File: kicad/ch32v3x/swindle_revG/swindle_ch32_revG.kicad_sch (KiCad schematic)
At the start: 34 parts, among them J1 jtag, J2 Conn_01x03_Socket, J2_DFU1 con2, J3 Dbg, J4 USB, J5 Debug port, U1 CH32V303RCT6, U2 LM1117-3.3, U3 3V->VTREF, U4 VTREF->3V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

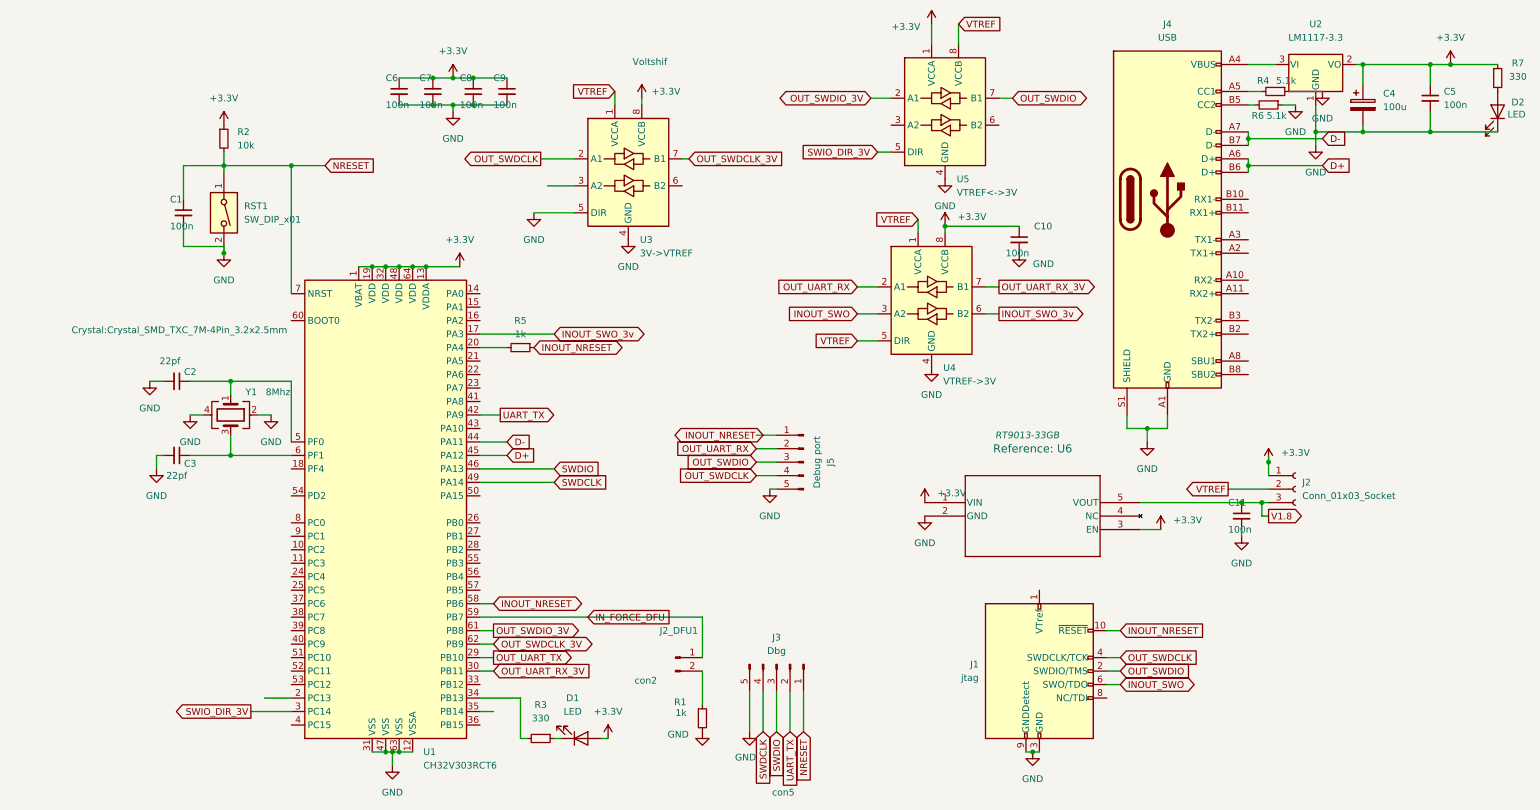
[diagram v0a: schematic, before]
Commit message: RP2040 : Add USE_RP2040 option to use the new PCB Kicad : RP2040 carrier layout mon : add mon enablereset to make exec from RAM work with vscode. That ignores the reset command sent by cortexdebug Misc : dont hardcode the target in the attach/vAttch command to 1.  Actually read the value.
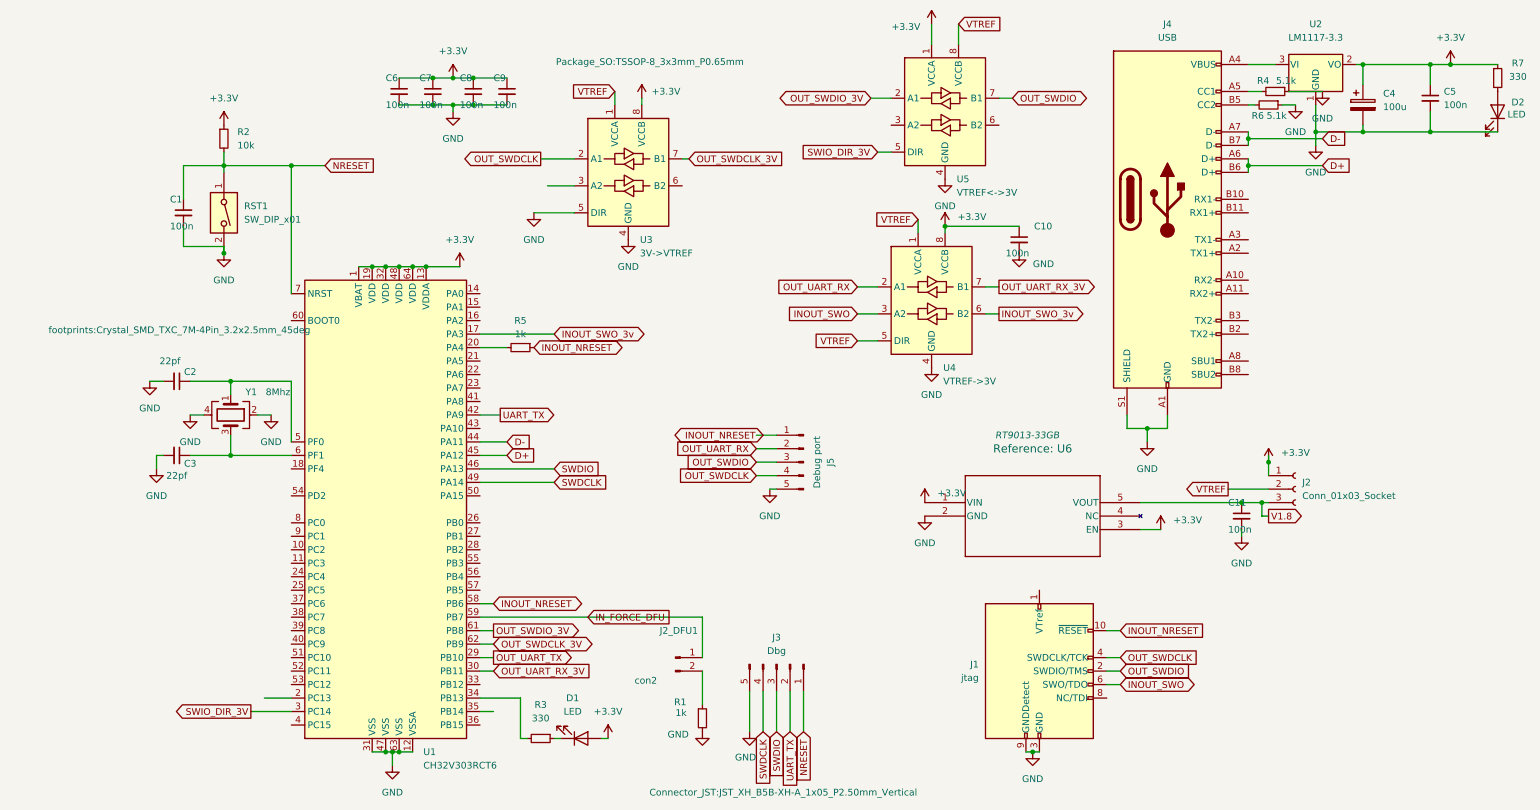
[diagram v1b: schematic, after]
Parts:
- J3: footprint con5 -> Connector_JST:JST_XH_B5B-XH-A_1x05_P2.50mm_Vertical
- J5: footprint Con5 -> Connector_JST:JST_XH_B5B-XH-A_1x05_P2.50mm_Vertical
- U3: footprint Voltshif -> Package_SO:TSSOP-8_3x3mm_P0.65mm
- U4, U5: footprint Package_SO:VSSOP-8_2.3x2mm_P0.5mm -> Package_SO:TSSOP-8_3x3mm_P0.65mm
- Y1: footprint Crystal:Crystal_SMD_TXC_7M-4Pin_3.2x2.5mm -> footprints:Crystal_SMD_TXC_7M-4Pin_3.2x2.5mm_45deg
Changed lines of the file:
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@@
 			)
 		)
-		(property "Footprint" "Con5"
+		(property "Footprint" "Connector_JST:JST_XH_B5B-XH-A_1x05_P2.50mm_Vertical"
 			(at 147.828 112.268 0)
 			(effects
@@
 			)
 		)
-		(property "Footprint" "Package_SO:VSSOP-8_2.3x2mm_P0.5mm"
+		(property "Footprint" "Package_SO:TSSOP-8_3x3mm_P0.65mm"
 			(at 175.26 46.99 0)
 			(effects
@@
 		)
 		(instances
-			(project "lnBMP_ch32_revF_5pins_prot"
+			(project "swindle_ch32_revG"
 				(path "/fbe443d6-6d74-4abc-9dee-16e0160553bc"
 					(reference "U5")
@@
 			)
 		)
-		(property "Footprint" "Voltshif"
+		(property "Footprint" "Package_SO:TSSOP-8_3x3mm_P0.65mm"
 			(at 118.364 23.622 0)
 			(effects
@@
 		)
 		(instances
-			(project "lnBMP_ch32_revF_5pins_prot"
+			(project "swindle_ch32_revG"
 				(path "/fbe443d6-6d74-4abc-9dee-16e0160553bc"
 					(reference "#PWR032")
@@
 		)
 		(instances
-			(project "lnBMP_ch32_revF_5pins_prot"
+			(project "swindle_ch32_revG"
 				(path "/fbe443d6-6d74-4abc-9dee-16e0160553bc"
 					(reference "#PWR026")
@@
 		)
 		(instances
-			(project "lnBMP_ch32_revF_5pins_prot"
+			(project "swindle_ch32_revG"
 				(path "/fbe443d6-6d74-4abc-9dee-16e0160553bc"
 					(reference "#PWR028")
@@
 		)
 		(instances
-			(project "lnBMP_ch32_revF_5pins_prot"
+			(project "swindle_ch32_revG"
 				(path "/fbe443d6-6d74-4abc-9dee-16e0160553bc"
 					(reference "C10")
@@
 		)
 		(instances
-			(project "lnBMP_ch32_revF_5pins_prot"
+			(project "swindle_ch32_revG"
 				(path "/fbe443d6-6d74-4abc-9dee-16e0160553bc"
 					(reference "#PWR030")
@@
 		)
 		(instances
-			(project "lnBMP_ch32_revF_5pins_prot"
+			(project "swindle_ch32_revG"
 				(path "/fbe443d6-6d74-4abc-9dee-16e0160553bc"
 					(reference "#PWR027")
@@
 			)
 		)
-		(property "Footprint" "Package_SO:VSSOP-8_2.3x2mm_P0.5mm"
+		(property "Footprint" "Package_SO:TSSOP-8_3x3mm_P0.65mm"
 			(at 172.72 82.55 0)
 			(effects
@@
 		)
 		(instances
-			(project "lnBMP_ch32_revF_5pins_prot"
+			(project "swindle_ch32_revG"
 				(path "/fbe443d6-6d74-4abc-9dee-16e0160553bc"
 					(reference "U4")
@@
 		)
 		(instances
-			(project "lnBMP_ch32_revF_5pins_prot"
+			(project "swindle_ch32_revG"
 				(path "/fbe443d6-6d74-4abc-9dee-16e0160553bc"
 					(reference "D2")
@@
 		)
 		(instances
-			(project "lnBMP_ch32_revF_5pins_prot"
+			(project "swindle_ch32_revG"
 				(path "/fbe443d6-6d74-4abc-9dee-16e0160553bc"
 					(reference "#PWR01")
@@
 		)
 		(instances
-			(project "lnBMP_ch32_revF_5pins_prot"
+			(project "swindle_ch32_revG"
 				(path "/fbe443d6-6d74-4abc-9dee-16e0160553bc"
 					(reference "#PWR031")
@@
 		)
 		(instances
-			(project "lnBMP_ch32_revF_5pins_prot"
+			(project "swindle_ch32_revG"
 				(path "/fbe443d6-6d74-4abc-9dee-16e0160553bc"
 					(reference "C11")
@@
 		)
 		(instances
-			(project "lnBMP_ch32_revF_5pins_prot"
+			(project "swindle_ch32_revG"
 				(path "/fbe443d6-6d74-4abc-9dee-16e0160553bc"
 					(reference "#PWR021")
@@
 			)
 		)
-		(property "Footprint" "con5"
+		(property "Footprint" "Connector_JST:JST_XH_B5B-XH-A_1x05_P2.50mm_Vertical"
 			(at 143.51 161.29 90)
 			(effects
@@
 		)
 		(instances
-			(project "lnBMP_ch32_revF_5pins_prot"
+			(project "swindle_ch32_revG"
 				(path "/fbe443d6-6d74-4abc-9dee-16e0160553bc"
 					(reference "#PWR022")
@@
 		)
 		(instances
-			(project "lnBMP_ch32_revF_5pins_prot"
+			(project "swindle_ch32_revG"
 				(path "/fbe443d6-6d74-4abc-9dee-16e0160553bc"
 					(reference "#PWR033")
@@
 		)
 		(instances
-			(project "lnBMP_ch32_revF_5pins_prot"
+			(project "swindle_ch32_revG"
 				(path "/fbe443d6-6d74-4abc-9dee-16e0160553bc"
 					(reference "#PWR023")
@@
 		)
 		(instances
-			(project "lnBMP_ch32_revF_5pins_prot"
+			(project "swindle_ch32_revG"
 				(path "/fbe443d6-6d74-4abc-9dee-16e0160553bc"
 					(reference "#PWR029")
@@
 		)
 		(instances
-			(project "lnBMP_ch32_revF_5pins_prot"
+			(project "swindle_ch32_revG"
 				(path "/fbe443d6-6d74-4abc-9dee-16e0160553bc"
 					(reference "#PWR025")
@@
 		)
 		(instances
-			(project "lnBMP_ch32_revF_5pins_prot"
+			(project "swindle_ch32_revG"
 				(path "/fbe443d6-6d74-4abc-9dee-16e0160553bc"
 					(reference "#PWR024")
@@
 		)
 		(instances
-			(project "lnBMP_ch32_revF_5pins_prot"
+			(project "swindle_ch32_revG"
 				(path "/fbe443d6-6d74-4abc-9dee-16e0160553bc"
 					(reference "#PWR011")
@@
 			)
 		)
-		(property "Footprint" "Crystal:Crystal_SMD_TXC_7M-4Pin_3.2x2.5mm"
+		(property "Footprint" "footprints:Crystal_SMD_TXC_7M-4Pin_3.2x2.5mm_45deg"
 			(at 29.718 74.168 90)
 			(effects
@@
 		)
 		(instances
-			(project "lnBMP_ch32_revF_5pins_prot"
+			(project "swindle_ch32_revG"
 				(path "/fbe443d6-6d74-4abc-9dee-16e0160553bc"
 					(reference "Y1")
@@
 		)
 		(instances
-			(project "lnBMP_ch32_revF_5pins_prot"
+			(project "swindle_ch32_revG"
 				(path "/fbe443d6-6d74-4abc-9dee-16e0160553bc"
 					(reference "R7")

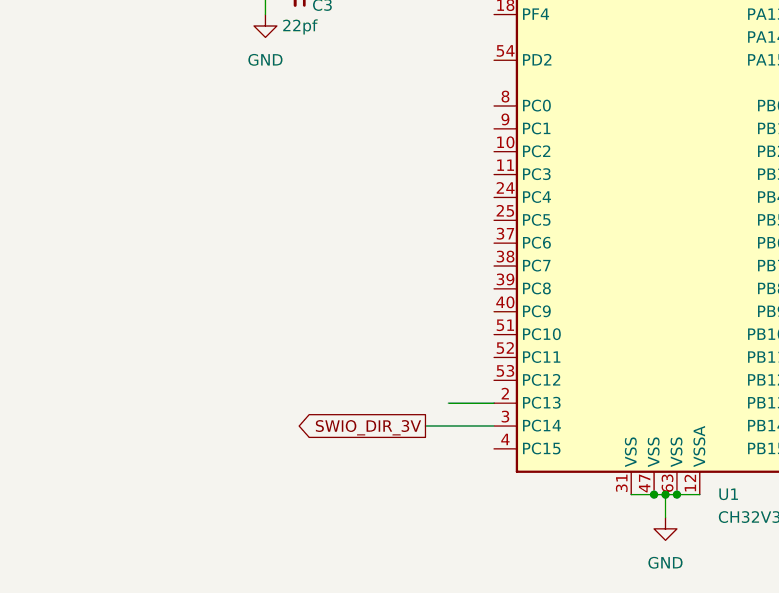
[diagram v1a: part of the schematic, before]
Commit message: kicad : use PC3 instead of PC14, which is not usable as GPIO on ch32v2/3
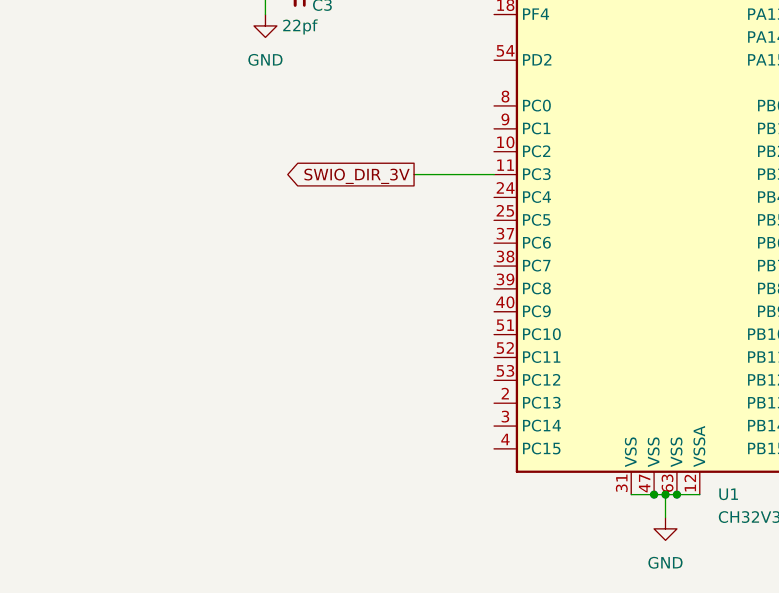
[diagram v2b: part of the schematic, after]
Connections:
- net SWIO_DIR_3V: now also U1.11 (PC3); no longer U1.3 (PC14)
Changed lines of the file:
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@@
-	(wire
-		(pts
-			(xy 45.72 143.51) (xy 50.8 143.51)
-		)
-		(stroke
-			(width 0)
-			(type default)
-		)
-	)
 	(wire
 		(pts
@@
 	(wire
 		(pts
-			(xy 43.18 146.05) (xy 50.8 146.05)
-		)
-		(stroke
-			(width 0)
-			(type default)
-		)
-	)
-	(wire
-		(pts
 			(xy 138.43 99.06) (xy 142.24 99.06)
 		)
@@
 		(pts
 			(xy 231.14 31.75) (xy 232.41 31.75)
+		)
+		(stroke
+			(width 0)
+			(type default)
+		)
+	)
+	(wire
+		(pts
+			(xy 41.91 118.11) (xy 50.8 118.11)
 		)
 		(stroke
@@
 	(global_label "SWIO_DIR_3V"
 		(shape output)
-		(at 43.18 146.05 180)
+		(at 41.91 118.11 180)
 		(fields_autoplaced yes)
 		(effects
@@
 		)
 		(property "Intersheetrefs" "${INTERSHEET_REFS}"
-			(at 28.2205 146.05 0)
+			(at 26.9505 118.11 0)
 			(effects
 				(font
